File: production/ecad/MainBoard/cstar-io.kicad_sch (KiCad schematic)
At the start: 11 parts, among them J1 691137710002, J5 Conn_01x04_Socket, Q2 AO3400A, Q8 IRFHM9331TRPBF

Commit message: Power footprints done
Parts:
- C11: footprint (none) -> Capacitor_SMD:C_0805_2012Metric
- R28: footprint (none) -> Resistor_SMD:R_0805_2012Metric
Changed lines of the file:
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@@
     )
     (pin "1")
+    (pin "2")
+    (pin "3")
     (pin "4")
+    (pin "5")
+    (pin "6")
     (pin "7")
-    (pin "6")
-    (pin "3")
     (pin "8")
-    (pin "5")
-    (pin "2")
     (instances
       (project "cstar-io"
@@
       (effects (font (size 1.27 1.27)) hide)
     )
+    (pin "1")
     (pin "2")
     (pin "3")
     (pin "4")
-    (pin "1")
     (instances
       (project "cstar-io"
@@
       (effects (font (size 1.27 1.27)) (justify left))
     )
-    (property "Footprint" "" (at 204.47 71.12 0)
+    (property "Footprint" "Capacitor_SMD:C_0805_2012Metric" (at 204.47 71.12 0)
       (effects (font (size 1.27 1.27)) hide)
     )
@@
       (effects (font (size 1.27 1.27)) hide)
     )
-    (pin "2")
-    (pin "1")
+    (pin "1")
+    (pin "2")
     (instances
       (project "cstar-io"
@@
       (effects (font (size 1.27 1.27) italic) hide)
     )
-    (pin "2")
-    (pin "1")
+    (pin "1")
+    (pin "2")
     (instances
       (project "cstar-io"
@@
       (effects (font (size 1.27 1.27)) (justify left))
     )
-    (property "Footprint" "" (at 199.771 85.344 90)
+    (property "Footprint" "Resistor_SMD:R_0805_2012Metric" (at 199.771 85.344 90)
       (effects (font (size 1.27 1.27)) hide)
     )
@@
       (effects (font (size 1.27 1.27)) hide)
     )
-    (pin "2")
-    (pin "1")
-    (instances
-      (project "cstar-io"
+    (pin "1")
+    (pin "2")
+    (instances
+      (project "cstar-io"

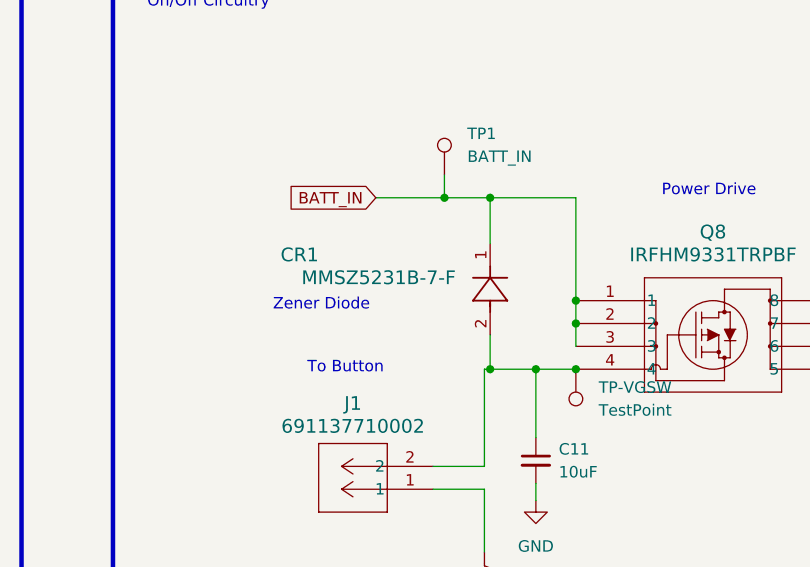
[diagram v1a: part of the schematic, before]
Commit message: footprint assignments
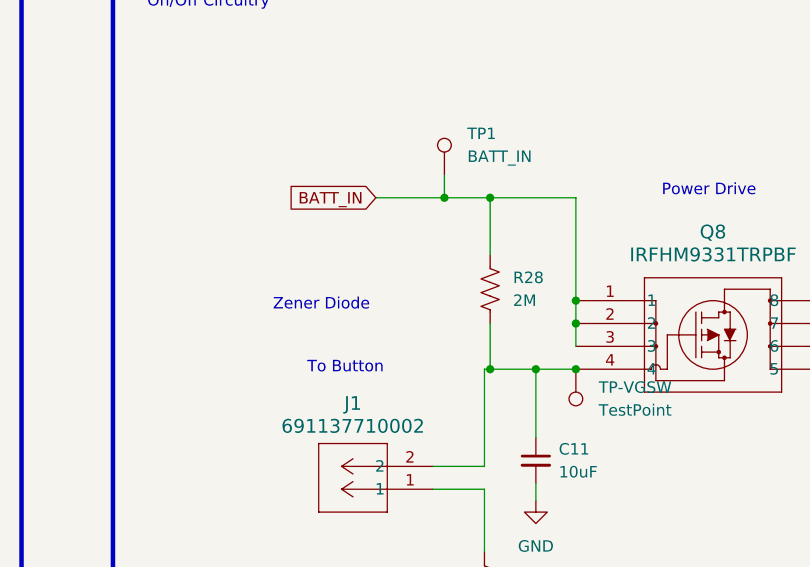
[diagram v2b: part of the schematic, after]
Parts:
- removed CR1: MMSZ5231B-7-F, SOD123_DIO, symbol 2024-02-24_22-47-34:MMSZ5231B-7-F
- added R28: 2M, Resistor_SMD:R_0805_2012Metric, symbol Device:R_US
- J1: footprint CONN2_710002_WRE -> CSTAR-MainBoard-Footprints:691137710002-2CONN
- J5: footprint (none) -> CSTAR-MainBoard-Footprints:B4B_PH_K_S
- Q8: footprint PG-TSDSON-8-902_INF -> CSTAR-MainBoard-Footprints:IRFHM9331TRPBF
- TP-VGSW, TP1: footprint (none) -> TestPoint:TestPoint_Pad_D2.0mm
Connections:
- net BATT_IN: now also R28.1
- net at C11.1, J1.2, Q8.4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: now also R28.2
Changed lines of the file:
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@@
     (stroke (width 0) (type default))
   )
-  (wire (pts (xy 199.39 41.91) (xy 199.39 46.99))
+  (wire (pts (xy 199.39 41.91) (xy 199.39 48.26))
     (stroke (width 0) (type default))
   )
@@
     (stroke (width 0.5) (type default))
   )
-  (wire (pts (xy 199.39 57.15) (xy 199.39 60.96))
+  (wire (pts (xy 199.39 55.88) (xy 199.39 60.96))
     (stroke (width 0) (type default))
   )
@@
       (effects (font (size 1.524 1.524)))
     )
-    (property "Footprint" "PG-TSDSON-8-902_INF" (at 208.915 53.34 0)
+    (property "Footprint" "CSTAR-MainBoard-Footprints:IRFHM9331TRPBF" (at 208.915 53.34 0)
       (effects (font (size 1.27 1.27) italic) hide)
     )
@@
       (project "CSTAR"
         (path "/cd9fa943-c6eb-468b-990c-ea873c442553/222d3537-e437-4ced-92e0-9423c8895d91"
-          (reference "Q12") (unit 1)
+          (reference "Q8") (unit 1)
         )
       )
@@
       (project "CSTAR"
         (path "/cd9fa943-c6eb-468b-990c-ea873c442553/222d3537-e437-4ced-92e0-9423c8895d91"
-          (reference "#PWR0134") (unit 1)
-        )
-      )
-    )
-  )
-  (symbol (lib_id "2024-02-24_22-47-34:MMSZ5231B-7-F") (at 199.39 57.15 90) (unit 1)
-    (in_bom yes) (on_board yes) (dnp no)
-    (property "Reference" "CR1" (at 180.34 48.26 90)
-      (effects (font (size 1.524 1.524)) (justify left))
-    )
-    (property "Value" "MMSZ5231B-7-F" (at 195.58 50.8 90)
-      (effects (font (size 1.524 1.524)) (justify left))
-    )
-    (property "Footprint" "SOD123_DIO" (at 199.39 57.15 0)
-      (effects (font (size 1.27 1.27) italic) hide)
-    )
-    (property "Datasheet" "MMSZ5231B-7-F" (at 199.39 57.15 0)
-      (effects (font (size 1.27 1.27) italic) hide)
-    )
-    (pin "1")
-    (pin "2")
-    (instances
-      (project "cstar-io"
-        (path "/62407770-7c51-469d-bef6-28d7dddfde53"
-          (reference "CR1") (unit 1)
-        )
-      )
-      (project "CSTAR"
-        (path "/cd9fa943-c6eb-468b-990c-ea873c442553/222d3537-e437-4ced-92e0-9423c8895d91"
-          (reference "CR3") (unit 1)
+          (reference "#PWR0126") (unit 1)
         )
       )
@@
       (project "CSTAR"
         (path "/cd9fa943-c6eb-468b-990c-ea873c442553/222d3537-e437-4ced-92e0-9423c8895d91"
-          (reference "#PWR0135") (unit 1)
+          (reference "#PWR0127") (unit 1)
         )
       )
@@
       (effects (font (size 1.27 1.27)) (justify left))
     )
-    (property "Footprint" "" (at 122.555 43.815 0)
+    (property "Footprint" "CSTAR-MainBoard-Footprints:B4B_PH_K_S" (at 122.555 43.815 0)
       (effects (font (size 1.27 1.27)) hide)
     )
@@
         )
         (path "/cd9fa943-c6eb-468b-990c-ea873c442553/222d3537-e437-4ced-92e0-9423c8895d91"
-          (reference "Q11") (unit 1)
+          (reference "Q7") (unit 1)
         )
       )
@@
       (effects (font (size 1.27 1.27)) (justify left))
     )
-    (property "Footprint" "" (at 199.39 39.37 0)
+    (property "Footprint" "TestPoint:TestPoint_Pad_D2.0mm" (at 199.39 39.37 0)
       (effects (font (size 1.27 1.27)) hide)
     )
@@
       (project "CSTAR"
         (path "/cd9fa943-c6eb-468b-990c-ea873c442553/222d3537-e437-4ced-92e0-9423c8895d91"
-          (reference "C34") (unit 1)
+          (reference "C38") (unit 1)
         )
       )
@@
       (project "CSTAR"
         (path "/cd9fa943-c6eb-468b-990c-ea873c442553/222d3537-e437-4ced-92e0-9423c8895d91"
-          (reference "#PWR0137") (unit 1)
+          (reference "#PWR0129") (unit 1)
         )
       )
@@
       (project "CSTAR"
         (path "/cd9fa943-c6eb-468b-990c-ea873c442553/222d3537-e437-4ced-92e0-9423c8895d91"
-          (reference "#PWR0131") (unit 1)
+          (reference "#PWR0123") (unit 1)
         )
       )
@@
         )
         (path "/cd9fa943-c6eb-468b-990c-ea873c442553/222d3537-e437-4ced-92e0-9423c8895d91"
-          (reference "Q9") (unit 1)
+          (reference "Q5") (unit 1)
         )
       )
@@
       (project "CSTAR"
         (path "/cd9fa943-c6eb-468b-990c-ea873c442553/222d3537-e437-4ced-92e0-9423c8895d91"
-          (reference "#PWR0132") (unit 1)
+          (reference "#PWR0124") (unit 1)
         )
       )
@@
       (project "CSTAR"
         (path "/cd9fa943-c6eb-468b-990c-ea873c442553/222d3537-e437-4ced-92e0-9423c8895d91"
-          (reference "#PWR0133") (unit 1)
+          (reference "#PWR0125") (unit 1)
+        )
+      )
+    )
+  )
+  (symbol (lib_id "Device:R_US") (at 199.39 52.07 0) (unit 1)
+    (in_bom yes) (on_board yes) (dnp no) (fields_autoplaced)
+    (property "Reference" "R28" (at 201.93 50.8 0)
+      (effects (font (size 1.27 1.27)) (justify left))
+    )
+    (property "Value" "2M" (at 201.93 53.34 0)
+      (effects (font (size 1.27 1.27)) (justify left))
+    )
+    (property "Footprint" "Resistor_SMD:R_0805_2012Metric" (at 200.406 52.324 90)
+      (effects (font (size 1.27 1.27)) hide)
+    )
+    (property "Datasheet" "~" (at 199.39 52.07 0)
+      (effects (font (size 1.27 1.27)) hide)
+    )
+    (pin "1")
+    (pin "2")
+    (instances
+      (project "cstar-io"
+        (path "/62407770-7c51-469d-bef6-28d7dddfde53"
+          (reference "R28") (unit 1)
+        )
+      )
+      (project "CSTAR"
+        (path "/cd9fa943-c6eb-468b-990c-ea873c442553/222d3537-e437-4ced-92e0-9423c8895d91"
+          (reference "R47") (unit 1)
         )
       )
@@
       (effects (font (size 1.524 1.524)))
     )
-    (property "Footprint" "CONN2_710002_WRE" (at 193.04 74.295 0)
+    (property "Footprint" "CSTAR-MainBoard-Footprints:691137710002-2CONN" (at 193.04 74.295 0)
       (effects (font (size 1.27 1.27) italic) hide)
     )
@@
       (effects (font (size 1.27 1.27)) (justify right))
     )
-    (property "Footprint" "" (at 203.835 60.96 0)
+    (property "Footprint" "TestPoint:TestPoint_Pad_D2.0mm" (at 203.835 60.96 0)
       (effects (font (size 1.27 1.27)) hide)
     )
@@
       (project "CSTAR"
         (path "/cd9fa943-c6eb-468b-990c-ea873c442553/222d3537-e437-4ced-92e0-9423c8895d91"
-          (reference "R64") (unit 1)
+          (reference "R46") (unit 1)
         )
       )
@@
         )
         (path "/cd9fa943-c6eb-468b-990c-ea873c442553/222d3537-e437-4ced-92e0-9423c8895d91"
-          (reference "Q10") (unit 1)
+          (reference "Q6") (unit 1)
         )
       )
@@
       (project "CSTAR"
         (path "/cd9fa943-c6eb-468b-990c-ea873c442553/222d3537-e437-4ced-92e0-9423c8895d91"
-          (reference "#PWR0136") (unit 1)
-        )
-      )
+          (reference "#PWR0128") (unit 1)
+        )
+      )

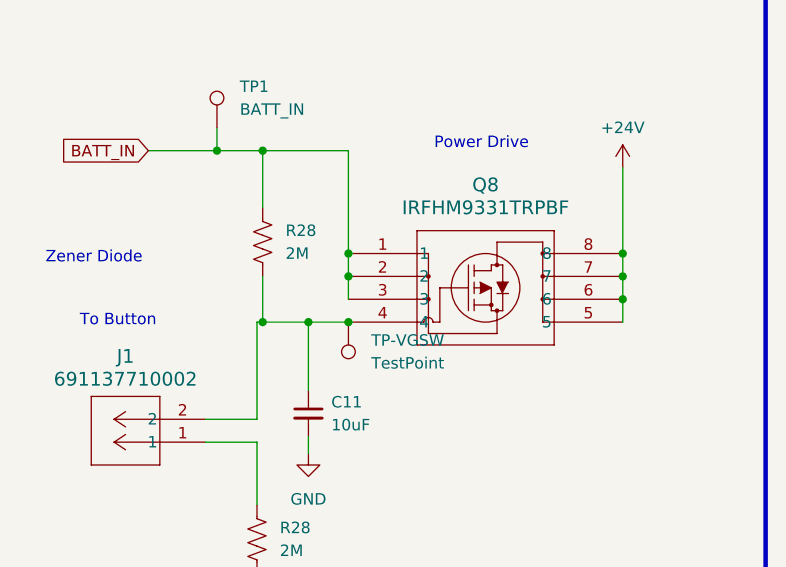
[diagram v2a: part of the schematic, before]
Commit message: footprint assign more
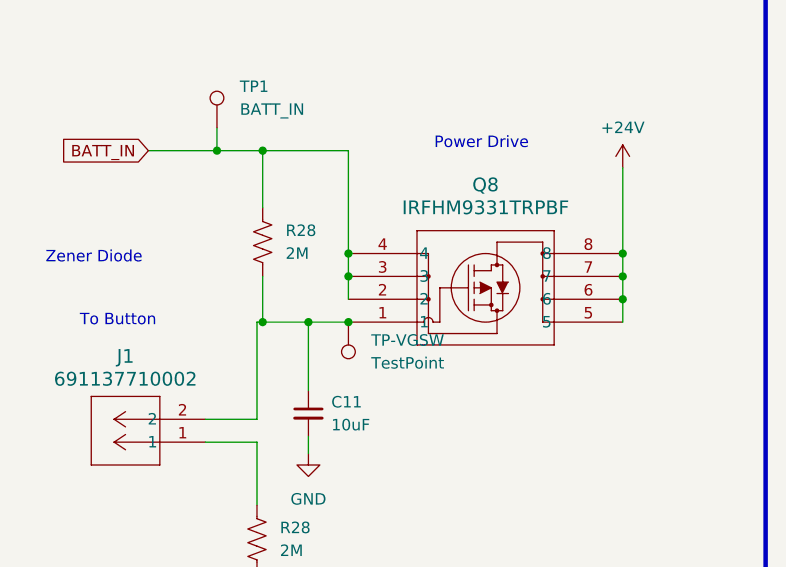
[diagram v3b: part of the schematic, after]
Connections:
- net BATT_IN: now also Q8.4; no longer Q8.1
- net at C11.1, J1.2, R28.2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: now also Q8.1; no longer Q8.4

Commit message: MORE LAYOUT and some schematic changes
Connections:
- net RBG_Green_Control renamed RGB_Green_Control
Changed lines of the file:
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@@
     (effects (font (size 1.27 1.27)) (justify left bottom))
+  )
+  (global_label "RGB_Green_Control" (shape input) (at 76.835 75.565 180) (fields_autoplaced)
+    (effects (font (size 1.27 1.27)) (justify right))
+    (property "Intersheetrefs" "${INTERSHEET_REFS}" (at 55.8281 75.565 0)
+      (effects (font (size 1.27 1.27)) (justify right) hide)
+    )
+  )
+  (global_label "RGB_Blue_Control" (shape input) (at 100.965 92.075 180) (fields_autoplaced)
+    (effects (font (size 1.27 1.27)) (justify right))
+    (property "Intersheetrefs" "${INTERSHEET_REFS}" (at 81.1677 92.075 0)
+      (effects (font (size 1.27 1.27)) (justify right) hide)
+    )
   )
   (global_label "BATT_IN" (shape input) (at 186.69 41.91 180) (fields_autoplaced)
@@
     )
   )
-  (hierarchical_label "RGB_Red_Control" (shape input) (at 45.085 54.61 180) (fields_autoplaced)
+  (global_label "RGB_Red_Control" (shape input) (at 45.085 54.61 180) (fields_autoplaced)
     (effects (font (size 1.27 1.27)) (justify right))
-  )
-  (hierarchical_label "RBG_Green_Control" (shape input) (at 76.835 75.565 180) (fields_autoplaced)
-    (effects (font (size 1.27 1.27)) (justify right))
-  )
-  (hierarchical_label "RGB_Blue_Control" (shape input) (at 100.965 92.075 180) (fields_autoplaced)
-    (effects (font (size 1.27 1.27)) (justify right))
+    (property "Intersheetrefs" "${INTERSHEET_REFS}" (at 25.9529 54.61 0)
+      (effects (font (size 1.27 1.27)) (justify right) hide)
+    )
   )
   (symbol (lib_id "IRFHM9331TRPBF:IRFHM9331TRPBF") (at 208.915 53.34 0) (unit 1)
